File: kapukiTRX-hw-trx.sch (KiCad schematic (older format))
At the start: 25 parts, among them J1 GPS, J2 SWD, U1 STM32L476RGTx, U2 LP38693-3.3, Y1 16MHz

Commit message: Wiring sensors
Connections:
- wire segments 145 -> 148
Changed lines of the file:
@@
 Text HLabel 7950 1920 0    50   Output ~ 0
 CANEN
+Text Label 7500 4900 2    50   ~ 0
+VCCCPU
+Wire Wire Line
+	7550 4900 7000 4900
+$Comp
+L power:GND #PWR0111
+U 1 1 5DCA6379
+P 7450 5750
+F 0 "#PWR0111" H 7450 5500 50  0001 C CNN
+F 1 "GND" H 7455 5577 50  0000 C CNN
+F 2 "" H 7450 5750 50  0001 C CNN
+F 3 "" H 7450 5750 50  0001 C CNN
+	1    7450 5750
+	1    0    0    -1
+$EndComp
+Wire Wire Line
+	7450 5750 7450 5700
+Wire Wire Line
+	7450 5700 7550 5700
 $Sheet
-S 8000 5250 1700 1050
+S 7550 4750 1700 1050
 U 5DB88B39
 F0 "Sensors" 50
 F1 "sensors.sch" 50
+F2 "BMPINT" O R 9250 5250 50
+F3 "BNOINT" O R 9250 5600 50
+F4 "BNORESET" I R 9250 5150 50
+F5 "GND" I L 7550 5700 50
+F6 "VCC" I L 7550 4900 50
+F7 "SDA" B L 7550 5150 50
+F8 "SCL" I L 7550 5250 50
 $EndSheet
 $EndSCHEMATC

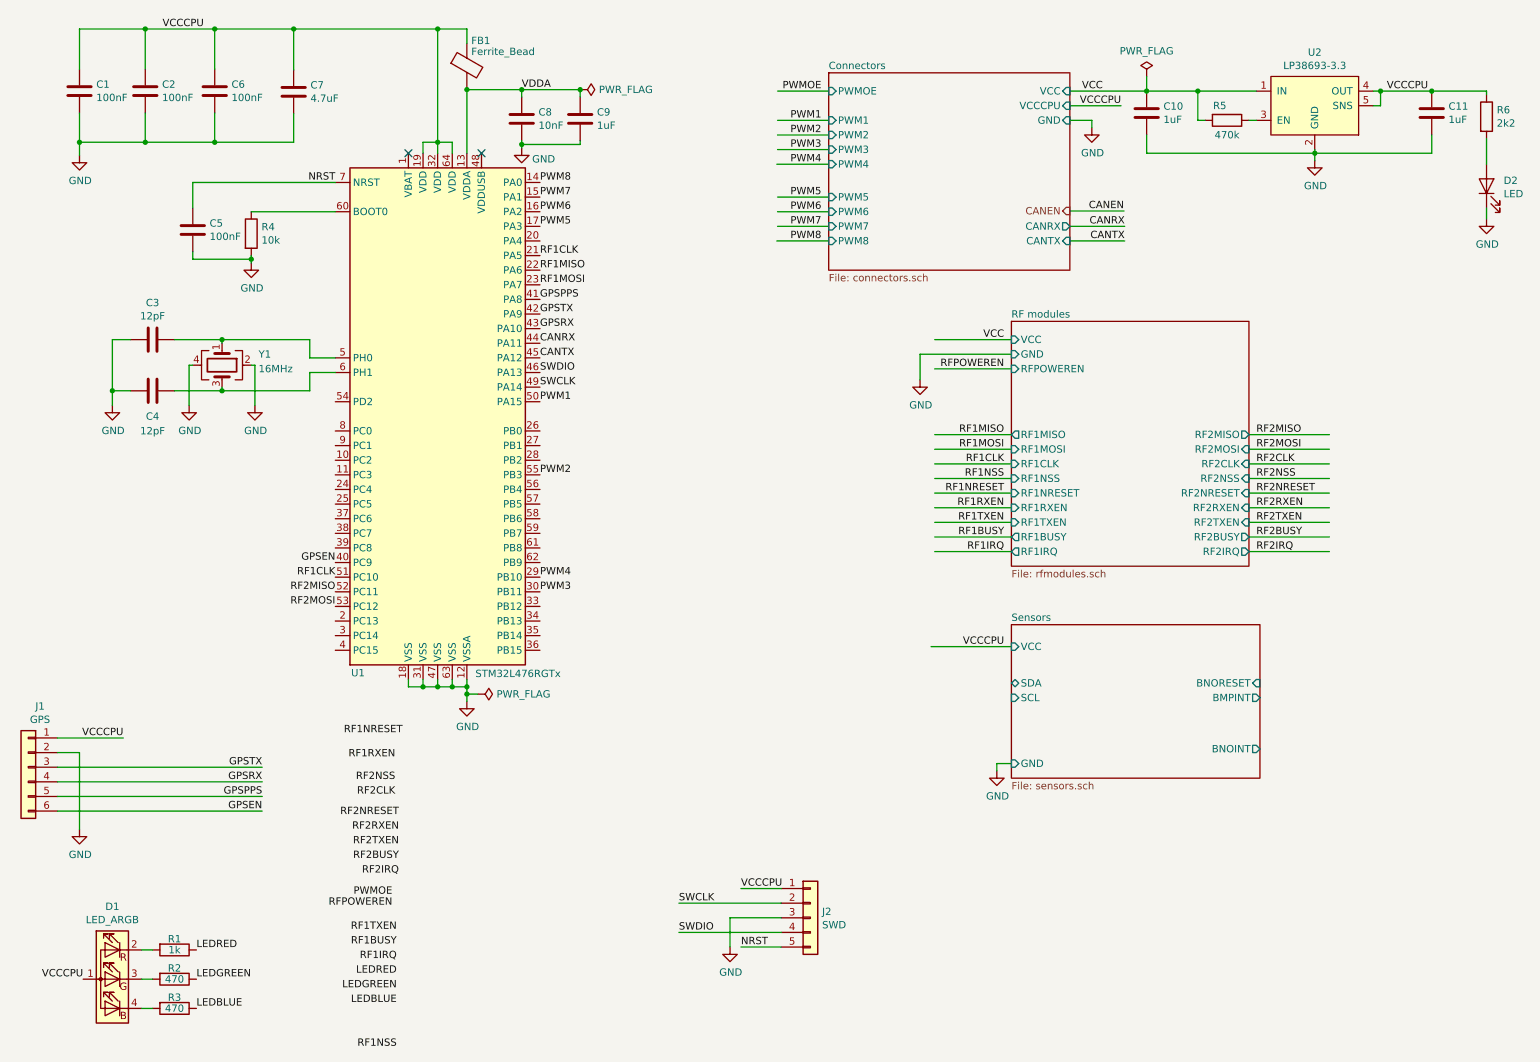
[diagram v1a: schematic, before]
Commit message: Change processor to G4 series
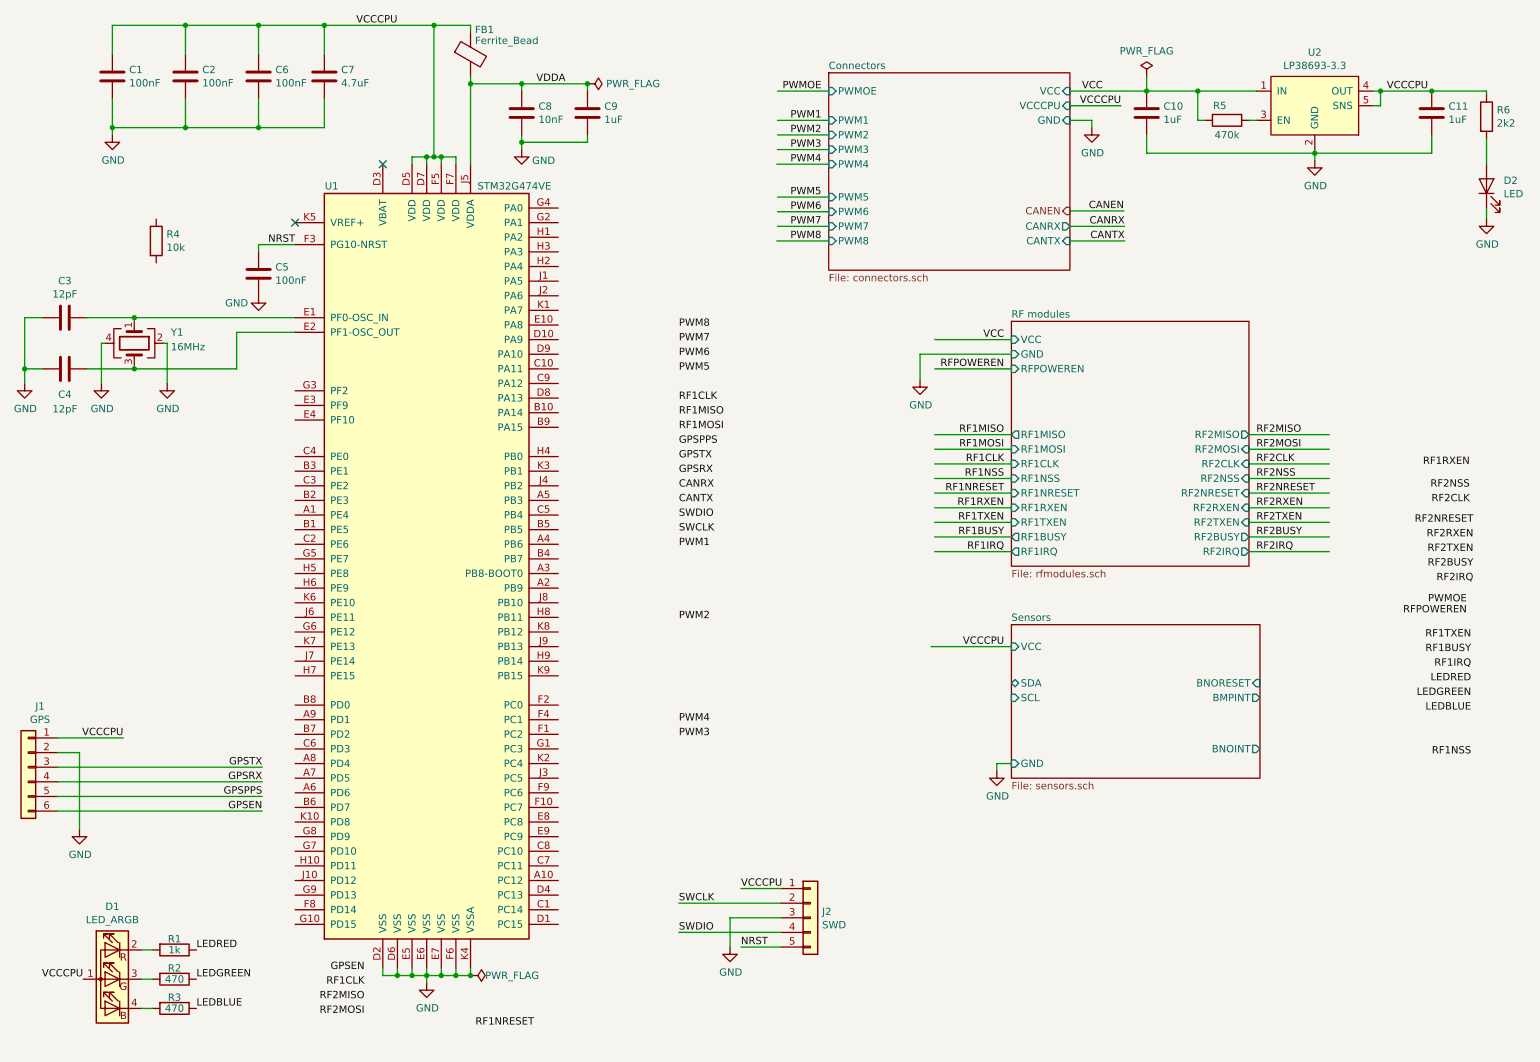
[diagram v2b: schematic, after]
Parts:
- removed U1: STM32L476RGTx, Package_QFP:LQFP-64_10x10mm_P0.5mm, symbol MCU_ST_STM32L4:STM32L476RGTx
- added U1: STM32G474VE, miscellaneous:TFBGA-100_10x10_8.0x8.0mm, symbol STM32G:STM32G474VE
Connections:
- wire segments 148 -> 146
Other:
- moved on the sheet: C1, C2, C3, C4, C5, C6, C7, C8, C9, FB1, R4, Y1

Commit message: Placing components and start routing
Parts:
- added JP?: SolderJumper_2_Open, symbol Jumper:SolderJumper_2_Open
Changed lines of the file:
@@
 U 1 1 5DD2FEBD
 P 3550 4300
-F 0 "U1" H 2900 6850 50  0000 C CNN
-F 1 "STM32G474VE" H 4150 6850 50  0000 C CNN
+F 0 "U1" H 3550 4400 50  0000 C CNN
+F 1 "STM32G474VE" H 3550 4300 50  0000 C CNN
 F 2 "miscellaneous:TFBGA-100_10x10_8.0x8.0mm" H 3550 4300 50  0001 C CNN
 F 3 "https://www.st.com/resource/en/datasheet/stm32g474cb.pdf" H 3550 4300 50  0001 C CNN
@@
 Wire Wire Line
 	1550 3000 2250 3000
-Text Label 2425 6025 2    50   ~ 0
+Text Label 1575 6025 2    50   ~ 0
 GPSEN
-Text Label 2425 5925 2    50   ~ 0
+Text Label 1575 5925 2    50   ~ 0
 GPSPPS
-Text Label 2425 5725 2    50   ~ 0
+Text Label 1575 5725 2    50   ~ 0
 GPSTX
-Text Label 2425 5825 2    50   ~ 0
+Text Label 1575 5825 2    50   ~ 0
 GPSRX
 Text Label 1475 5525 2    50   ~ 0
@@
 $EndComp
 Wire Wire Line
-	1025 6025 2425 6025
-Wire Wire Line
-	1025 5925 2425 5925
-Wire Wire Line
-	1025 5825 2425 5825
-Wire Wire Line
-	1025 5725 2425 5725
+	1025 6025 1575 6025
+Wire Wire Line
+	1025 5925 1575 5925
+Wire Wire Line
+	1025 5825 1575 5825
+Wire Wire Line
+	1025 5725 1575 5725
 $Comp
 L Connector_Generic:Conn_01x06 J1
@@
 	1    0    0    -1
 $EndComp
+$Comp
+L Jumper:SolderJumper_2_Open JP?
+U 1 1 5E0BD70F
+P 1200 4050
+F 0 "JP?" H 1200 4255 50  0000 C CNN
+F 1 "SolderJumper_2_Open" H 1200 4164 50  0000 C CNN
+F 2 "" H 1200 4050 50  0001 C CNN
+F 3 "~" H 1200 4050 50  0001 C CNN
+	1    1200 4050
+	1    0    0    -1
+$EndComp
